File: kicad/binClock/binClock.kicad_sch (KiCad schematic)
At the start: 55 parts, among them J1 Conn_02x04_Clockwise, J2 Conn_02x04_Clockwise, J3 Conn_02x04_Clockwise, J4 Conn_02x04_Clockwise, SW1 SW_Push, SW2 SW_Push, U3 ESP32-C3_SUPERMINI

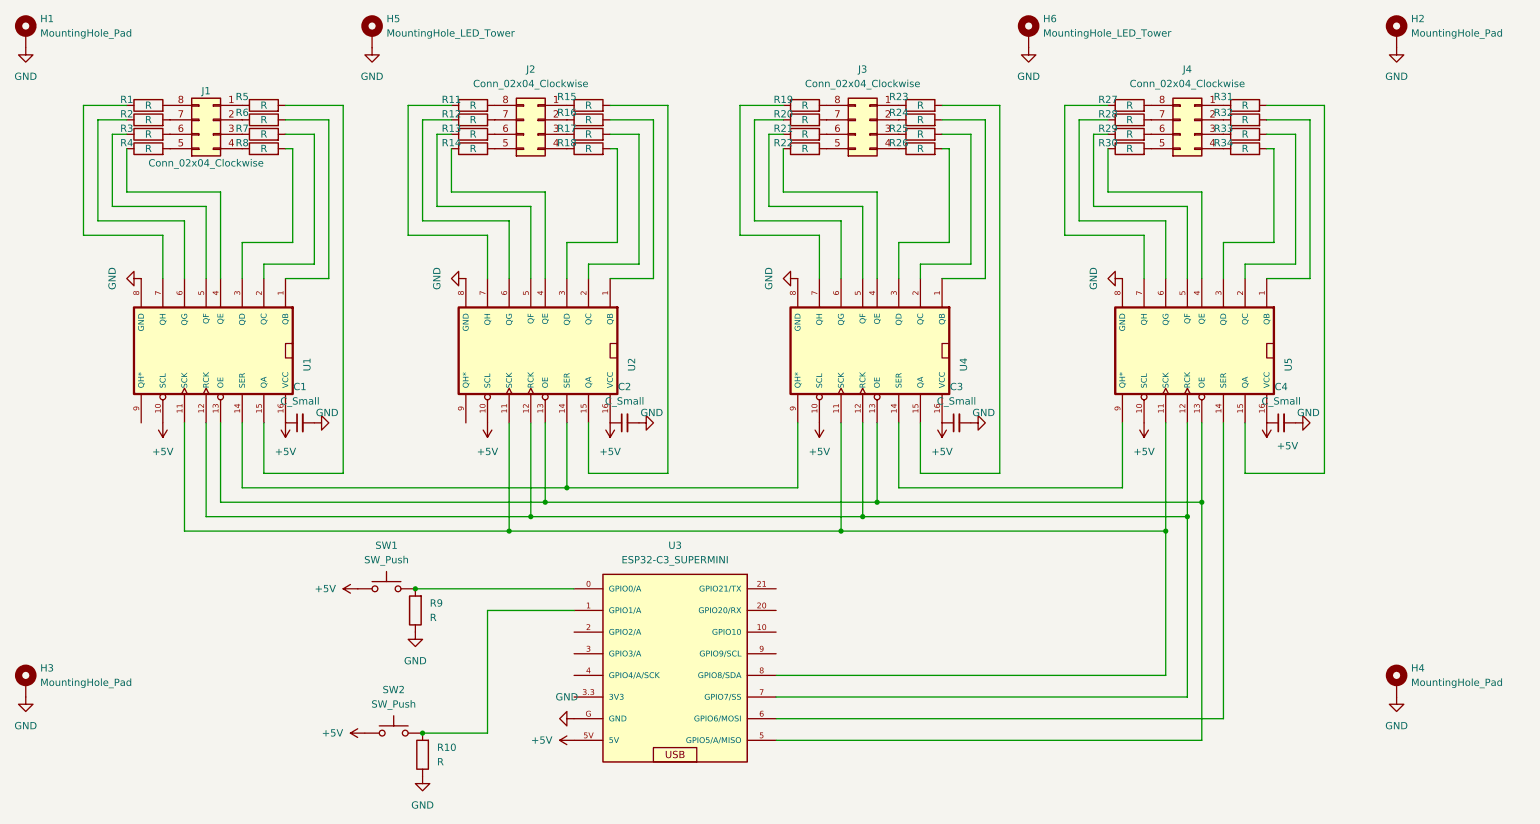
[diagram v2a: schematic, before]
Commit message: Added values to components. Added photo of assembled PCB and BOM
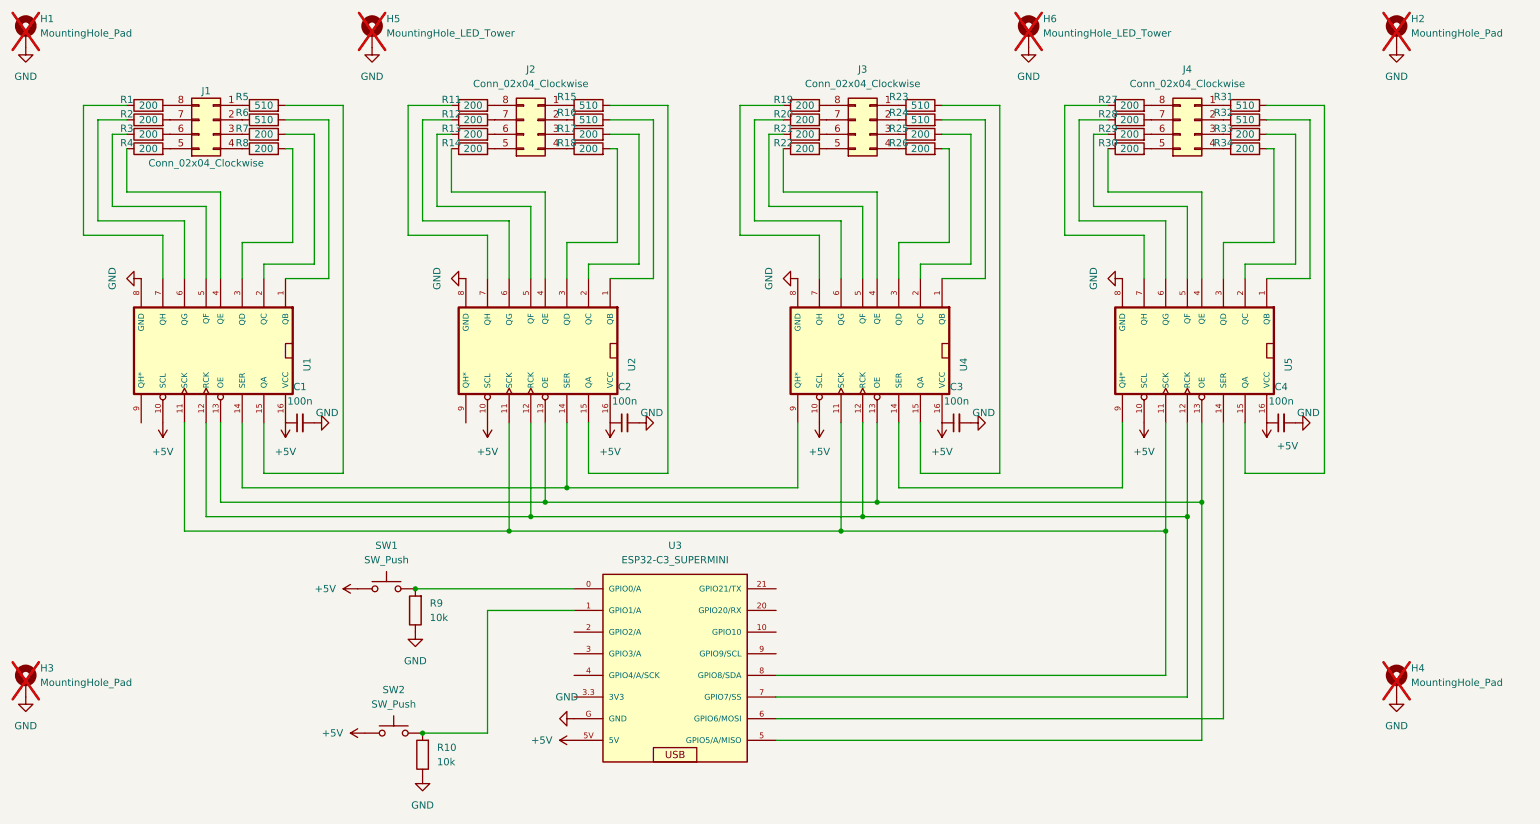
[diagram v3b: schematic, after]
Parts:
- C1, C2, C3, C4: value C_Small -> 100n
- H1, H2, H3, H4, H5, H6: now not fitted
- R1, R11, R12, R13, R14, R17, R18, R19, R2, R20, R21, R22, R25, R26, R27, R28, R29, R3, R30, R33, R34, R4, R7, R8: value R -> 200
- R10, R9: value R -> 10k
- R15, R16, R23, R24, R31, R32, R5, R6: value R -> 510
- U1, U2, U4, U5: value ~ -> 74HC595N
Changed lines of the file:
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@@
 			)
 		)
-		(property "Value" "R"
+		(property "Value" "200"
 			(at 219.71 44.45 90)
 			(effects
@@
 		(in_bom yes)
 		(on_board yes)
-		(dnp no)
+		(dnp yes)
 		(fields_autoplaced yes)
 		(property "Reference" "H3"
@@
 			)
 		)
-		(property "Value" "R"
+		(property "Value" "510"
 			(at 124.46 41.91 90)
 			(effects
@@
 			)
 		)
-		(property "Value" "R"
+		(property "Value" "200"
 			(at 162.56 41.91 90)
 			(effects
@@
 		(in_bom yes)
 		(on_board yes)
-		(dnp no)
+		(dnp yes)
 		(fields_autoplaced yes)
 		(property "Reference" "H5"
@@
 			)
 		)
-		(property "Value" "R"
+		(property "Value" "200"
 			(at 104.14 44.45 90)
 			(effects
@@
 			)
 		)
-		(property "Value" "R"
+		(property "Value" "200"
 			(at 46.99 39.37 90)
 			(effects
@@
 			)
 		)
-		(property "Value" "R"
+		(property "Value" "200"
 			(at 240.03 46.99 90)
 			(effects
@@
 			)
 		)
-		(property "Value" "R"
+		(property "Value" "200"
 			(at 182.88 46.99 90)
 			(effects
@@
 			)
 		)
-		(property "Value" "~"
+		(property "Value" "74HC595N"
 			(at 177.8 64.516 0)
 			(effects
@@
 			)
 		)
-		(property "Value" "R"
+		(property "Value" "200"
 			(at 162.56 44.45 90)
 			(effects
@@
 			)
 		)
-		(property "Value" "R"
+		(property "Value" "10k"
 			(at 96.52 129.5399 0)
 			(effects
@@
 			)
 		)
-		(property "Value" "C_Small"
+		(property "Value" "100n"
 			(at 73.6663 91.44 90)
 			(effects
@@
 			)
 		)
-		(property "Value" "R"
+		(property "Value" "200"
 			(at 46.99 46.99 90)
 			(effects
@@
 			)
 		)
-		(property "Value" "R"
+		(property "Value" "200"
 			(at 219.71 39.37 90)
 			(effects
@@
 			)
 		)
-		(property "Value" "R"
+		(property "Value" "200"
 			(at 219.71 46.99 90)
 			(effects
@@
 			)
 		)
-		(property "Value" "R"
+		(property "Value" "510"
 			(at 182.88 41.91 90)
 			(effects
@@
 			)
 		)
-		(property "Value" "C_Small"
+		(property "Value" "100n"
 			(at 246.3863 91.44 90)
 			(effects
@@
 			)
 		)
-		(property "Value" "R"
+		(property "Value" "200"
 			(at 182.88 44.45 90)
 			(effects
@@
 			)
 		)
-		(property "Value" "R"
+		(property "Value" "200"
 			(at 46.99 44.45 90)
 			(effects
@@
 			)
 		)
-		(property "Value" "R"
+		(property "Value" "200"
 			(at 67.31 46.99 90)
 			(effects
@@
 			)
 		)
-		(property "Value" "C_Small"
+		(property "Value" "100n"
 			(at 189.2363 91.44 90)
 			(effects
@@
 			)
 		)
-		(property "Value" "R"
+		(property "Value" "200"
 			(at 162.56 39.37 90)
 			(effects
@@
 			)
 		)
-		(property "Value" "R"
+		(property "Value" "200"
 			(at 104.14 46.99 90)
 			(effects
@@
 		(in_bom yes)
 		(on_board yes)
-		(dnp no)
+		(dnp yes)
 		(fields_autoplaced yes)
 		(property "Reference" "H2"
@@
 			)
 		)
-		(property "Value" "R"
+		(property "Value" "10k"
 			(at 97.79 154.9399 0)
 			(effects
@@
 			)
 		)
-		(property "Value" "R"
+		(property "Value" "200"
 			(at 104.14 39.37 90)
 			(effects
@@
 			)
 		)
-		(property "Value" "C_Small"
+		(property "Value" "100n"
 			(at 130.8163 91.44 90)
 			(effects
@@
 			)
 		)
-		(property "Value" "R"
+		(property "Value" "200"
 			(at 124.46 44.45 90)
 			(effects
@@
 			)
 		)
-		(property "Value" "R"
+		(property "Value" "510"
 			(at 67.31 39.37 90)
 			(effects
@@
 			)
 		)
-		(property "Value" "R"
+		(property "Value" "200"
 			(at 46.99 41.91 90)
 			(effects
@@
 			)
 		)
-		(property "Value" "R"
+		(property "Value" "510"
 			(at 124.46 39.37 90)
 			(effects
@@
 			)
 		)
-		(property "Value" "R"
+		(property "Value" "200"
 			(at 124.46 46.99 90)
 			(effects
@@
 		(in_bom yes)
 		(on_board yes)
-		(dnp no)
+		(dnp yes)
 		(fields_autoplaced yes)
 		(property "Reference" "H1"
@@
 			)
 		)
-		(property "Value" "R"
+		(property "Value" "200"
 			(at 67.31 44.45 90)
 			(effects
@@
 			)
 		)
-		(property "Value" "R"
+		(property "Value" "200"
 			(at 162.56 46.99 90)
 			(effects
@@
 			)
 		)
-		(property "Value" "R"
+		(property "Value" "200"
 			(at 219.71 41.91 90)
 			(effects
@@
 		(in_bom yes)
 		(on_board yes)
-		(dnp no)
+		(dnp yes)
 		(fields_autoplaced yes)
 		(property "Reference" "H6"
@@
 		(in_bom yes)
 		(on_board yes)
-		(dnp no)
+		(dnp yes)
 		(fields_autoplaced yes)
 		(property "Reference" "H4"
@@
 			)
 		)
-		(property "Value" "R"
+		(property "Value" "510"
 			(at 67.31 41.91 90)
 			(effects
@@
 			)
 		)
-		(property "Value" "R"
+		(property "Value" "510"
 			(at 240.03 41.91 90)
 			(effects
@@
 			)
 		)
-		(property "Value" "R"
+		(property "Value" "200"
 			(at 104.14 41.91 90)
 			(effects
@@
 			)
 		)
-		(property "Value" "~"
+		(property "Value" "74HC595N"
 			(at 62.23 64.516 0)
 			(effects
@@
 			)
 		)
-		(property "Value" "R"
+		(property "Value" "200"
 			(at 240.03 44.45 90)
 			(effects
@@
 			)
 		)
-		(property "Value" "~"
+		(property "Value" "74HC595N"
 			(at 119.38 64.516 0)
 			(effects
@@
 			)
 		)
-		(property "Value" "R"
+		(property "Value" "510"
 			(at 182.88 39.37 90)
 			(effects
@@
 			)
 		)
-		(property "Value" "R"
+		(property "Value" "510"
 			(at 240.03 39.37 90)
 			(effects
@@
 			)
 		)
-		(property "Value" "~"
+		(property "Value" "74HC595N"
 			(at 234.95 64.516 0)
 			(effects

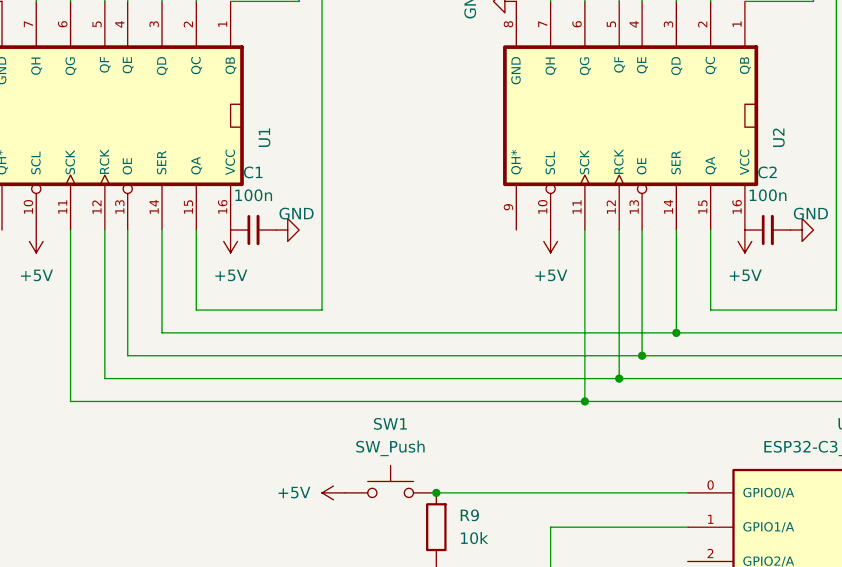
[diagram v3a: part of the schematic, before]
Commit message: Corrected error in schematic and recreated production files
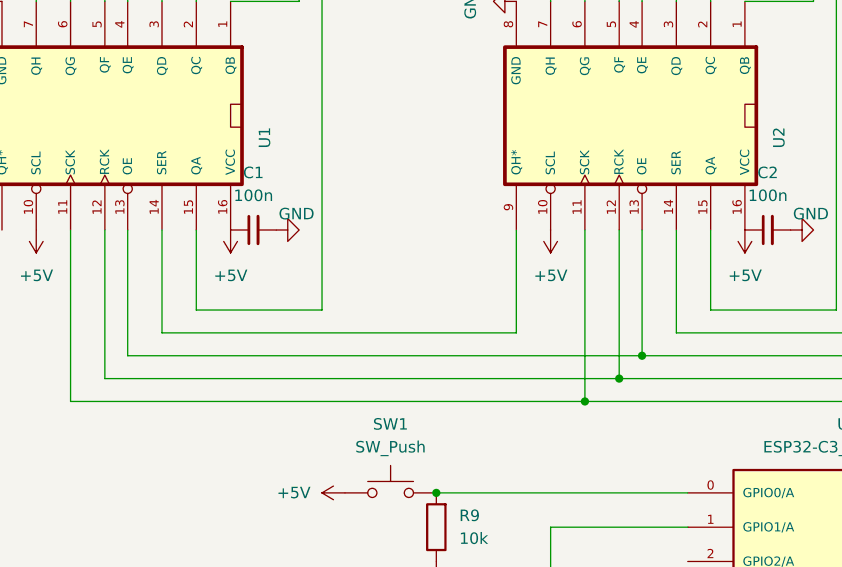
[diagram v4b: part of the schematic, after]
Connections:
- net at U2.14 (SER), U4.9 (QH*): no longer U1.14 (SER)
- net at U2.9 (QH*): now also U1.14 (SER)
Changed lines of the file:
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@@
-	)
-	(junction
-		(at 120.65 106.68)
-		(diameter 0)
-		(color 0 0 0 0)
 	)
 	(junction
@@
 	(wire
 		(pts
+			(xy 102.87 95.25) (xy 102.87 106.68)
+		)
+		(stroke
+			(width 0)
+			(type default)
+		)
+	)
+	(wire
+		(pts
 			(xy 133.35 44.45) (xy 128.27 44.45)
 		)
@@
 	(wire
 		(pts
+			(xy 102.87 106.68) (xy 63.5 106.68)
+		)
+		(stroke
+			(width 0)
+			(type default)
+		)
+	)
+	(wire
+		(pts
 			(xy 248.92 44.45) (xy 243.84 44.45)
 		)
@@
 		)
 		(stroke
-			(width 0)
-			(type default)
-		)
-	)
-	(wire
-		(pts
-			(xy 63.5 106.68) (xy 120.65 106.68)
-		)
-		(stroke
